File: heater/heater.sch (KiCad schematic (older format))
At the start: 9 parts, among them J1 power Input, J2 input uC, J3 thermostat, J4 to mcu, Q1 BC517

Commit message: heater done
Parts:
- removed J2: input uC, Socket_Strips:Socket_Strip_Straight_1x01_Pitch2.54mm, symbol Connector:Conn_01x01_Male
- removed J4: to mcu, Socket_Strips:Socket_Strip_Straight_1x01_Pitch2.54mm, symbol Connector:Conn_01x01_Male
- removed R1: 47, Resistors_THT:R_Axial_DIN0414_L11.9mm_D4.5mm_P15.24mm_Horizontal, symbol Device:R_US
- added J2: MCUpins, Connectors_JST:JST_XH_B03B-XH-A_03x2.50mm_Straight, symbol Connector:Conn_01x03_Male
- added J4: fan, Connectors_JST:JST_XH_B02B-XH-A_02x2.50mm_Straight, symbol Connector:Conn_01x02_Male
- added Q2: BC517, TO_SOT_Packages_THT:TO-92_Inline_Wide, symbol Transistor_BJT:BC517
- added R5: 1k, Resistors_SMD:R_0805_HandSoldering, symbol Device:R_US
- J1: footprint Connectors_JST:JST_EH_B04B-EH-A_04x2.50mm_Straight -> Connectors_JST:JST_XH_B04B-XH-A_04x2.50mm_Straight
- J3: value thermostat -> thermistor; footprint Socket_Strips:Socket_Strip_Straight_1x02_Pitch2.54mm -> Connectors_JST:JST_XH_B02B-XH-A_02x2.50mm_Straight
- R2: value 10 -> 27; footprint Resistors_THT:R_Axial_Power_L75.0mm_W9.0mm_P81.28mm -> Resistors_THT:R_Axial_Power_L38.0mm_W9.0mm_P40.64mm
- R3, R4: value R_US -> 1k
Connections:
- net +12V: now also J1.3 (Pin_3), R2.2, J4.1 (Pin_1); no longer J1.2 (Pin_2)
- net +5V: now also J1.2 (Pin_2); no longer J1.3 (Pin_3)
- net GND: now also J1.1 (Pin_1), Q2.3 (E); no longer J1.4 (Pin_4)
- net fromMcuR: now reaches R3.2
- net fromMcuR: now also J2.2 (Pin_2)
- net mcu renamed toMcu
- net toMcu: now also J2.3 (Pin_3)
- new net: J4.2 (Pin_2), Q2.1 (C)
- new net: Q2.2 (B), R5.1
- new net fromMcuF: J2.1 (Pin_1), R5.2
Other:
- moved on the sheet: J3, R4
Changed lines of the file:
@@
 P 3750 2050
 F 0 "R2" H 3818 2096 50  0000 L CNN
-F 1 "10" H 3818 2005 50  0000 L CNN
-F 2 "Resistors_THT:R_Axial_Power_L75.0mm_W9.0mm_P81.28mm" V 3790 2040 50  0001 C CNN
+F 1 "27" H 3818 2005 50  0000 L CNN
+F 2 "Resistors_THT:R_Axial_Power_L38.0mm_W9.0mm_P40.64mm" V 3790 2040 50  0001 C CNN
 F 3 "~" H 3750 2050 50  0001 C CNN
 	1    3750 2050
-	-1   0    0    1
-$EndComp
-$Comp
-L Device:R_US R1
-U 1 1 5C2F3120
-P 3750 1650
-F 0 "R1" H 3818 1696 50  0000 L CNN
-F 1 "47" H 3818 1605 50  0000 L CNN
-F 2 "Resistors_THT:R_Axial_DIN0414_L11.9mm_D4.5mm_P15.24mm_Horizontal" V 3790 1640 50  0001 C CNN
-F 3 "~" H 3750 1650 50  0001 C CNN
-	1    3750 1650
 	-1   0    0    1
 $EndComp
@@
 F 0 "J1" H 2050 2700 50  0000 L CNN
 F 1 "power Input" H 1800 2800 50  0000 L CNN
-F 2 "Connectors_JST:JST_EH_B04B-EH-A_04x2.50mm_Straight" H 2150 2500 50  0001 C CNN
+F 2 "Connectors_JST:JST_XH_B04B-XH-A_04x2.50mm_Straight" H 2150 2500 50  0001 C CNN
 F 3 "~" H 2150 2500 50  0001 C CNN
 	1    2150 2500
 	1    0    0    -1
 $EndComp
-Wire Wire Line
-	1950 2500 1750 2500
-Wire Wire Line
-	1950 2600 1750 2600
-Wire Wire Line
-	1950 2700 1750 2700
 Text Label 1750 2500 2    50   ~ 0
-+12V
-Text Label 1750 2600 2    50   ~ 0
 +5V
 $Comp
 L power:GND #PWR0101
 U 1 1 5C303485
-P 1750 2700
-F 0 "#PWR0101" H 1750 2450 50  0001 C CNN
-F 1 "GND" H 1755 2527 50  0000 C CNN
-F 2 "" H 1750 2700 50  0001 C CNN
-F 3 "" H 1750 2700 50  0001 C CNN
-	1    1750 2700
-	1    0    0    -1
-$EndComp
-NoConn ~ 1950 2400
+P 1850 2250
+F 0 "#PWR0101" H 1850 2000 50  0001 C CNN
+F 1 "GND" H 1855 2077 50  0000 C CNN
+F 2 "" H 1850 2250 50  0001 C CNN
+F 3 "" H 1850 2250 50  0001 C CNN
+	1    1850 2250
+	1    0    0    -1
+$EndComp
 $Comp
 L Transistor_BJT:BC517 Q1
@@
 $EndComp
 $Comp
-L Connector:Conn_01x01_Male J2
-U 1 1 5C307D7B
-P 2500 2500
-F 0 "J2" H 2606 2678 50  0000 C CNN
-F 1 "input uC" H 2606 2587 50  0000 C CNN
-F 2 "Socket_Strips:Socket_Strip_Straight_1x01_Pitch2.54mm" H 2500 2500 50  0001 C CNN
-F 3 "~" H 2500 2500 50  0001 C CNN
-	1    2500 2500
-	1    0    0    -1
-$EndComp
-$Comp
 L Device:R_US R3
 U 1 1 5C307DD4
 P 3050 2500
 F 0 "R3" H 3118 2546 50  0000 L CNN
-F 1 "R_US" H 3118 2455 50  0000 L CNN
+F 1 "1k" H 3118 2455 50  0000 L CNN
 F 2 "Resistors_SMD:R_0805_HandSoldering" V 3090 2490 50  0001 C CNN
 F 3 "~" H 3050 2500 50  0001 C CNN
@@
 	3200 2500 3450 2500
 Wire Wire Line
-	3750 1800 3750 1900
-Wire Wire Line
-	3750 2200 3750 2300
-Wire Wire Line
-	3750 1500 3750 1400
+	3750 2700 3750 3100
+$Comp
+L power:GND #PWR0103
+U 1 1 5C308243
+P 3750 3100
+F 0 "#PWR0103" H 3750 2850 50  0001 C CNN
+F 1 "GND" H 3755 2927 50  0000 C CNN
+F 2 "" H 3750 3100 50  0001 C CNN
+F 3 "" H 3750 3100 50  0001 C CNN
+	1    3750 3100
+	1    0    0    -1
+$EndComp
+$Comp
+L Connector:Conn_01x02_Male J3
+U 1 1 5C308B5A
+P 6650 2250
+F 0 "J3" H 6623 2130 50  0000 R CNN
+F 1 "thermistor" H 6623 2221 50  0000 R CNN
+F 2 "Connectors_JST:JST_XH_B02B-XH-A_02x2.50mm_Straight" H 6650 2250 50  0001 C CNN
+F 3 "~" H 6650 2250 50  0001 C CNN
+	1    6650 2250
+	-1   0    0    1
+$EndComp
+Wire Wire Line
+	6450 2250 6350 2250
+$Comp
+L Device:R_US R4
+U 1 1 5C336026
+P 6350 1650
+F 0 "R4" H 6418 1696 50  0000 L CNN
+F 1 "1k" H 6418 1605 50  0000 L CNN
+F 2 "Resistors_SMD:R_0805_HandSoldering" V 6390 1640 50  0001 C CNN
+F 3 "~" H 6350 1650 50  0001 C CNN
+	1    6350 1650
+	1    0    0    -1
+$EndComp
+$Comp
+L power:GND #PWR0104
+U 1 1 5C3360BC
+P 6350 3100
+F 0 "#PWR0104" H 6350 2850 50  0001 C CNN
+F 1 "GND" H 6355 2927 50  0000 C CNN
+F 2 "" H 6350 3100 50  0001 C CNN
+F 3 "" H 6350 3100 50  0001 C CNN
+	1    6350 3100
+	1    0    0    -1
+$EndComp
+Wire Wire Line
+	6450 2150 6350 2150
+Wire Wire Line
+	6350 2150 6350 1950
+$Comp
+L power:+5V #PWR0105
+U 1 1 5C33660C
+P 6350 1400
+F 0 "#PWR0105" H 6350 1250 50  0001 C CNN
+F 1 "+5V" H 6365 1573 50  0000 C CNN
+F 2 "" H 6350 1400 50  0001 C CNN
+F 3 "" H 6350 1400 50  0001 C CNN
+	1    6350 1400
+	1    0    0    -1
+$EndComp
+Wire Wire Line
+	6350 1400 6350 1500
+Wire Wire Line
+	6350 1950 6600 1950
+Connection ~ 6350 1950
+Text Label 6600 1950 0    50   ~ 0
+toMcu
+Text Label 2700 2500 2    50   ~ 0
+fromMcuR
+Wire Wire Line
+	2050 1800 2150 1800
+Wire Wire Line
+	2050 1900 2150 1900
+Text Label 2150 1800 0    50   ~ 0
+fromMcuR
+Text Label 2150 1900 0    50   ~ 0
+toMcu
+$Comp
+L Transistor_BJT:BC517 Q2
+U 1 1 5C346CA2
+P 5600 2500
+F 0 "Q2" H 5791 2546 50  0000 L CNN
+F 1 "BC517" H 5791 2455 50  0000 L CNN
+F 2 "TO_SOT_Packages_THT:TO-92_Inline_Wide" H 5800 2425 50  0001 L CIN
+F 3 "http://www.fairchildsemi.com/ds/BC/BC517.pdf" H 5600 2500 50  0001 L CNN
+	1    5600 2500
+	1    0    0    -1
+$EndComp
+$Comp
+L power:GND #PWR0106
+U 1 1 5C34725E
+P 5700 3100
+F 0 "#PWR0106" H 5700 2850 50  0001 C CNN
+F 1 "GND" H 5705 2927 50  0000 C CNN
+F 2 "" H 5700 3100 50  0001 C CNN
+F 3 "" H 5700 3100 50  0001 C CNN
+	1    5700 3100
+	1    0    0    -1
+$EndComp
+Wire Wire Line
+	5700 2700 5700 3100
+$Comp
+L Device:R_US R5
+U 1 1 5C3474DA
+P 5150 2500
+F 0 "R5" H 5218 2546 50  0000 L CNN
+F 1 "1k" H 5218 2455 50  0000 L CNN
+F 2 "Resistors_SMD:R_0805_HandSoldering" V 5190 2490 50  0001 C CNN
+F 3 "~" H 5150 2500 50  0001 C CNN
+	1    5150 2500
+	0    1    1    0
+$EndComp
+Wire Wire Line
+	5300 2500 5400 2500
+Wire Wire Line
+	6350 1950 6350 1800
+Wire Wire Line
+	5000 2500 4700 2500
+Text Label 4700 2500 2    50   ~ 0
+fromMcuF
+Wire Wire Line
+	6350 2250 6350 3100
+$Comp
+L Connector:Conn_01x02_Male J4
+U 1 1 5C34ABB8
+P 5150 1750
+F 0 "J4" H 5256 1928 50  0000 C CNN
+F 1 "fan" H 5256 1837 50  0000 C CNN
+F 2 "Connectors_JST:JST_XH_B02B-XH-A_02x2.50mm_Straight" H 5150 1750 50  0001 C CNN
+F 3 "~" H 5150 1750 50  0001 C CNN
+	1    5150 1750
+	1    0    0    -1
+$EndComp
+Wire Wire Line
+	5700 2300 5700 1850
+Wire Wire Line
+	5700 1850 5350 1850
+Text Label 1750 2600 2    50   ~ 0
++12V
 $Comp
 L power:+12V #PWR0102
@@
 $EndComp
 Wire Wire Line
-	3750 2700 3750 3100
-$Comp
-L power:GND #PWR0103
-U 1 1 5C308243
-P 3750 3100
-F 0 "#PWR0103" H 3750 2850 50  0001 C CNN
-F 1 "GND" H 3755 2927 50  0000 C CNN
-F 2 "" H 3750 3100 50  0001 C CNN
-F 3 "" H 3750 3100 50  0001 C CNN
-	1    3750 3100
-	1    0    0    -1
-$EndComp
-$Comp
-L Connector:Conn_01x02_Male J3
-U 1 1 5C308B5A
-P 5200 2250
-F 0 "J3" H 5173 2130 50  0000 R CNN
-F 1 "thermostat" H 5173 2221 50  0000 R CNN
-F 2 "Socket_Strips:Socket_Strip_Straight_1x02_Pitch2.54mm" H 5200 2250 50  0001 C CNN
-F 3 "~" H 5200 2250 50  0001 C CNN
-	1    5200 2250
-	-1   0    0    1
-$EndComp
-Wire Wire Line
-	5000 2250 4900 2250
-$Comp
-L Device:R_US R4
-U 1 1 5C336026
-P 4900 1650
-F 0 "R4" H 4968 1696 50  0000 L CNN
-F 1 "R_US" H 4968 1605 50  0000 L CNN
-F 2 "Resistors_SMD:R_0805_HandSoldering" V 4940 1640 50  0001 C CNN
-F 3 "~" H 4900 1650 50  0001 C CNN
-	1    4900 1650
-	1    0    0    -1
-$EndComp
-$Comp
-L power:GND #PWR0104
-U 1 1 5C3360BC
-P 4900 3150
-F 0 "#PWR0104" H 4900 2900 50  0001 C CNN
-F 1 "GND" H 4905 2977 50  0000 C CNN
-F 2 "" H 4900 3150 50  0001 C CNN
-F 3 "" H 4900 3150 50  0001 C CNN
-	1    4900 3150
-	1    0    0    -1
-$EndComp
-Wire Wire Line
-	5000 2150 4900 2150
-Wire Wire Line
-	4900 2150 4900 1950
-Wire Wire Line
-	4900 2250 4900 3150
-$Comp
-L power:+5V #PWR0105
-U 1 1 5C33660C
-P 4900 1400
-F 0 "#PWR0105" H 4900 1250 50  0001 C CNN
-F 1 "+5V" H 4915 1573 50  0000 C CNN
-F 2 "" H 4900 1400 50  0001 C CNN
-F 3 "" H 4900 1400 50  0001 C CNN
-	1    4900 1400
-	1    0    0    -1
-$EndComp
-Wire Wire Line
-	4900 1400 4900 1500
-Wire Wire Line
-	4900 1950 5150 1950
-Connection ~ 4900 1950
-Wire Wire Line
-	4900 1950 4900 1800
-Text Label 5000 1950 0    50   ~ 0
-mcu
-$Comp
-L Connector:Conn_01x01_Male J4
-U 1 1 5C336DF5
-P 5350 1950
-F 0 "J4" H 5323 1880 50  0000 R CNN
-F 1 "to mcu" H 5323 1971 50  0000 R CNN
-F 2 "Socket_Strips:Socket_Strip_Straight_1x01_Pitch2.54mm" H 5350 1950 50  0001 C CNN
-F 3 "~" H 5350 1950 50  0001 C CNN
-	1    5350 1950
-	-1   0    0    1
-$EndComp
+	5350 1750 5700 1750
+Wire Wire Line
+	5700 1750 5700 1500
+Wire Wire Line
+	5700 1500 3750 1500
+Wire Wire Line
+	3750 1400 3750 1500
+Wire Wire Line
+	3750 1500 3750 1900
+Connection ~ 3750 1500
+Wire Wire Line
+	3750 2200 3750 2300
+$Comp
+L Connector:Conn_01x03_Male J2
+U 1 1 5C350621
+P 1850 1800
+F 0 "J2" H 1956 2078 50  0000 C CNN
+F 1 "MCUpins" H 1956 1987 50  0000 C CNN
+F 2 "Connectors_JST:JST_XH_B03B-XH-A_03x2.50mm_Straight" H 1850 1800 50  0001 C CNN
+F 3 "~" H 1850 1800 50  0001 C CNN
+	1    1850 1800
+	1    0    0    -1
+$EndComp
+Wire Wire Line
+	2050 1700 2150 1700
+Text Label 2150 1700 0    50   ~ 0
+fromMcuF
+NoConn ~ 1950 2700
+Wire Wire Line
+	1750 2600 1950 2600
+Wire Wire Line
+	1750 2500 1950 2500
+Wire Wire Line
+	1950 2400 1950 2250
+Wire Wire Line
+	1950 2250 1850 2250
 $EndSCHEMATC

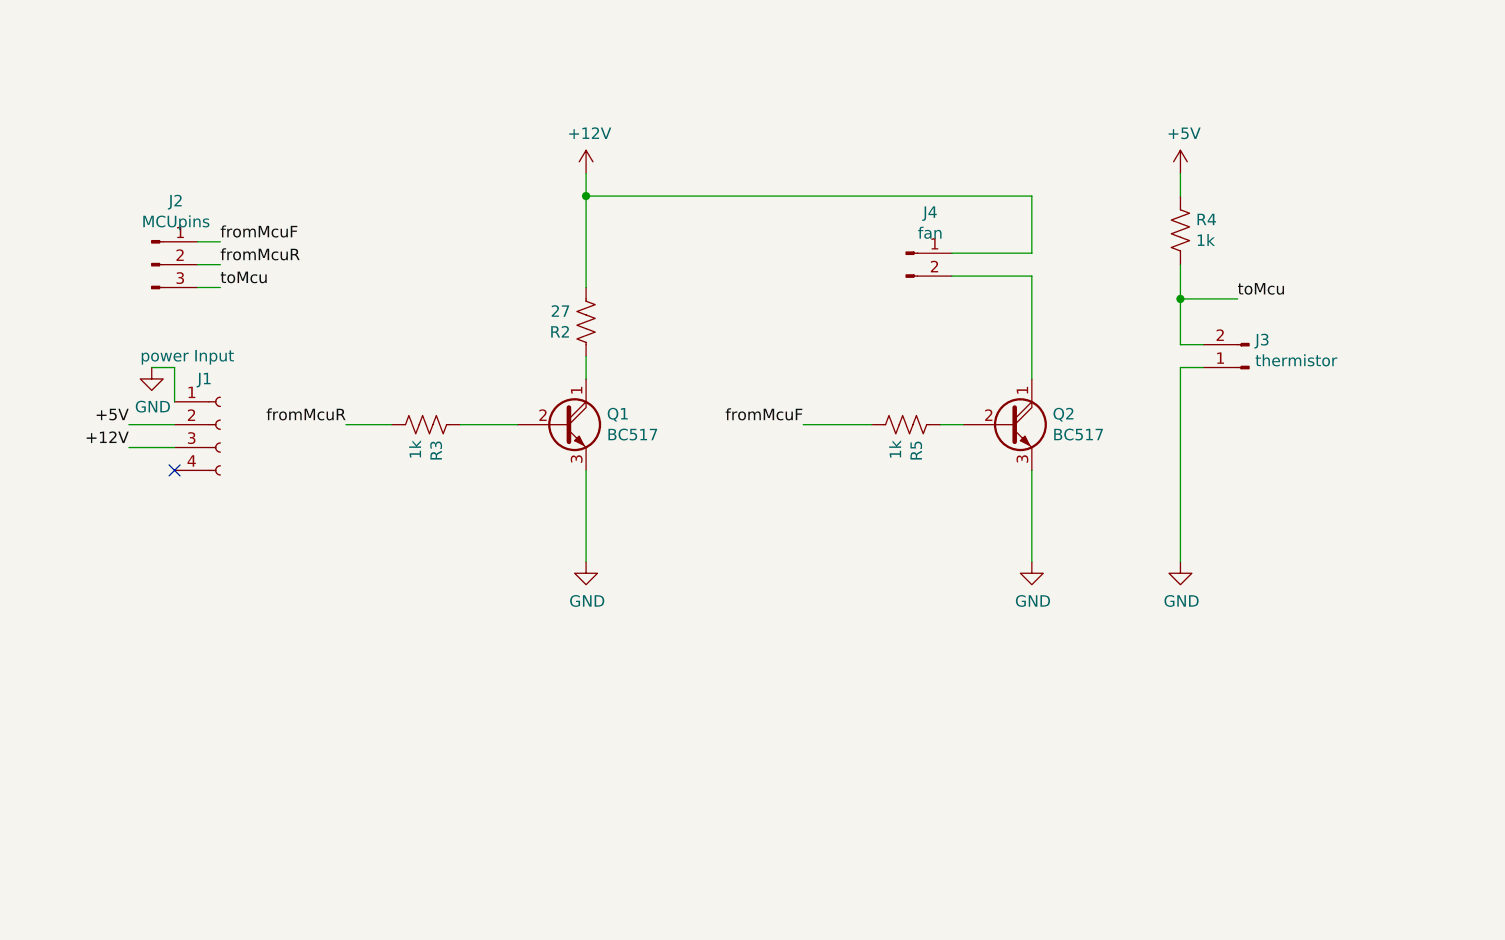
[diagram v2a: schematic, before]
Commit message: added indicator LED's in heater module; added proper markings in motor module.
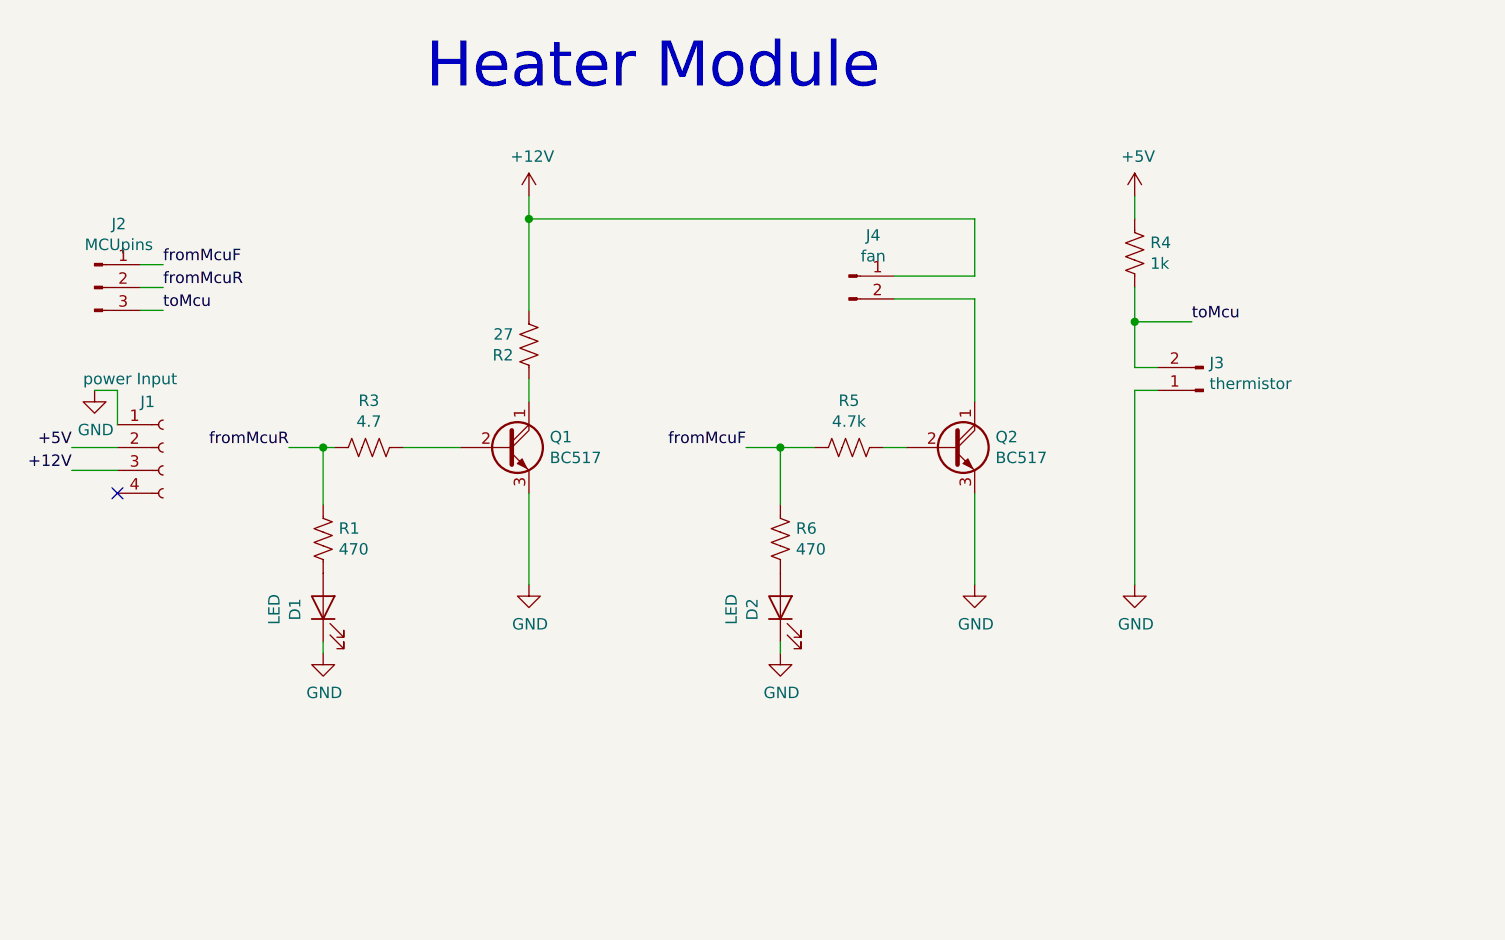
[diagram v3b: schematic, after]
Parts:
- added D1, D2: LED, LEDs:LED_0805_HandSoldering, symbol Device:LED
- added R1, R6: 470, Resistors_SMD:R_0805_HandSoldering, symbol Device:R_US
- R3: value 1k -> 4.7
- R5: value 1k -> 4.7k
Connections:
- net GND: now also D1.1 (K), D2.1 (K)
- net fromMcuF: now also R6.1
- net fromMcuR: now also R1.1
- new net: D1.2 (A), R1.2
- new net: D2.2 (A), R6.2
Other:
- note added: "Heater Module"
- moved on the sheet: J1, J2, J3, J4, Q1, Q2, R2, R3, R4, R5

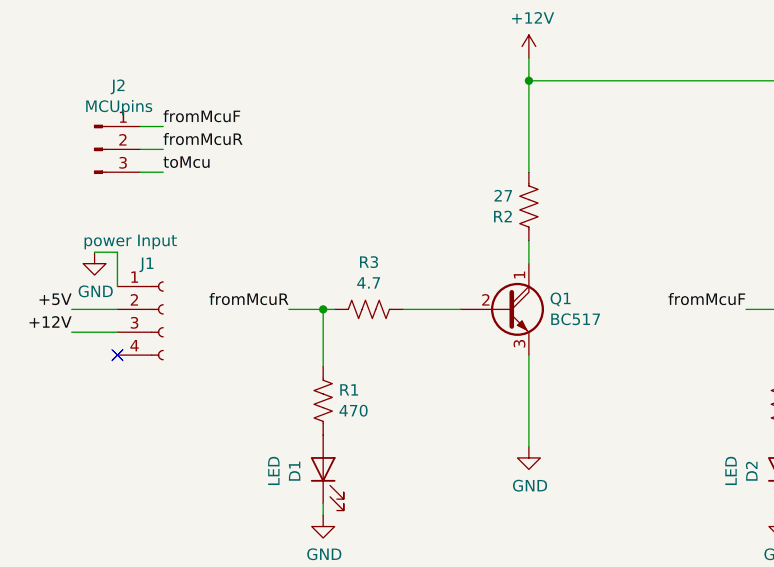
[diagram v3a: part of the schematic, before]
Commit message: swapped power and switch connector postions
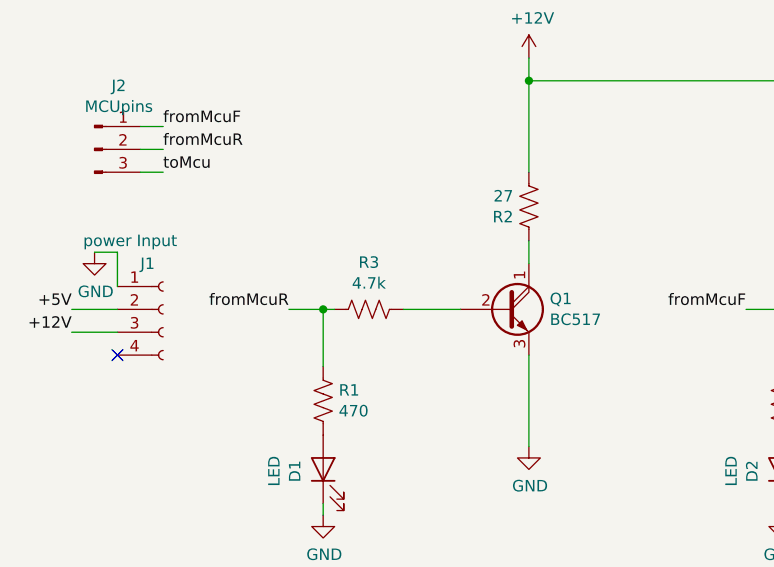
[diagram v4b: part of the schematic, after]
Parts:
- R3: value 4.7 -> 4.7k
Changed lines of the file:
@@
 P 2800 2600
 F 0 "R3" V 2595 2600 50  0000 C CNN
-F 1 "4.7" V 2686 2600 50  0000 C CNN
+F 1 "4.7k" V 2686 2600 50  0000 C CNN
 F 2 "Resistors_SMD:R_0805_HandSoldering" V 2840 2590 50  0001 C CNN
 F 3 "~" H 2800 2600 50  0001 C CNN
